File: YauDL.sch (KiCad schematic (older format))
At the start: 32 parts, among them K1 HEATSINK, Q1 IRLZ34N, Q2 IRLZ34N, Q3 AO3401, Q4 AO3401, SW1 SWITCH_INV, T1 Binding post, T2 Binding post, T3 Banana socket, T4 Banana socket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

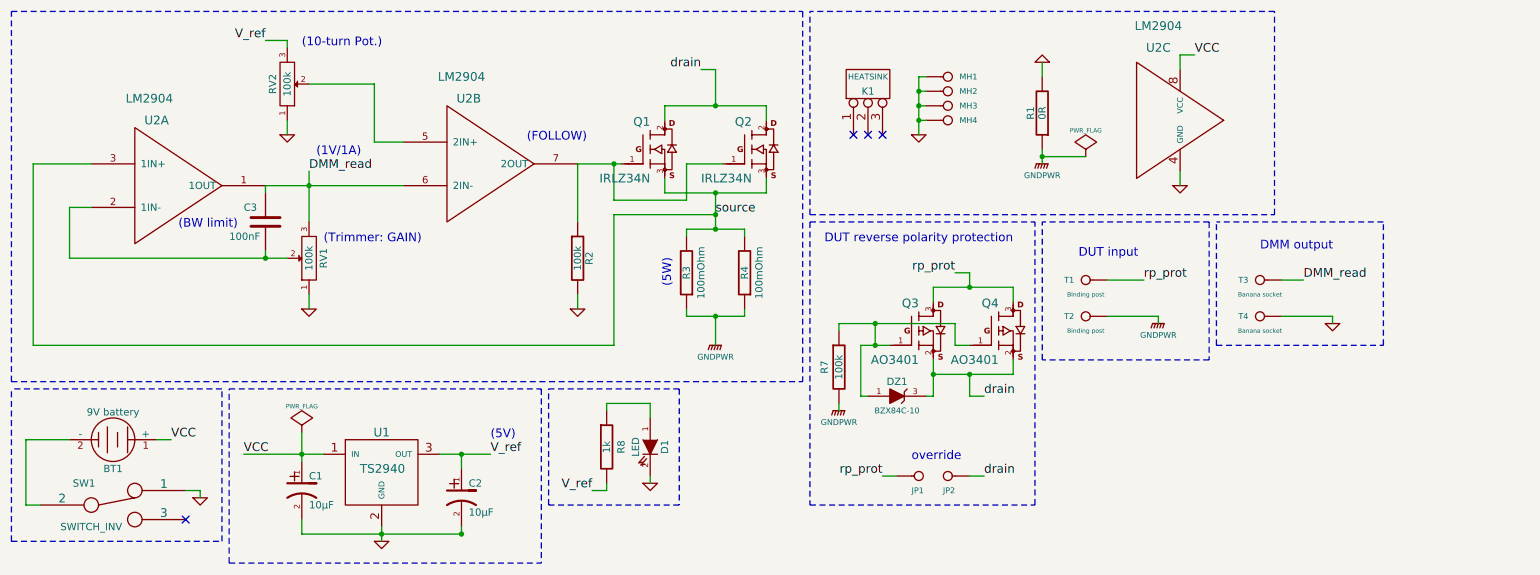
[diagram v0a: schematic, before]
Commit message: Added a low-pass filter (RC=100ms) to the output opamp.
LTSpice simulations indicated oscillation at higher currents.
Hopefully the real thing doesn't require it, but I can bodge it.
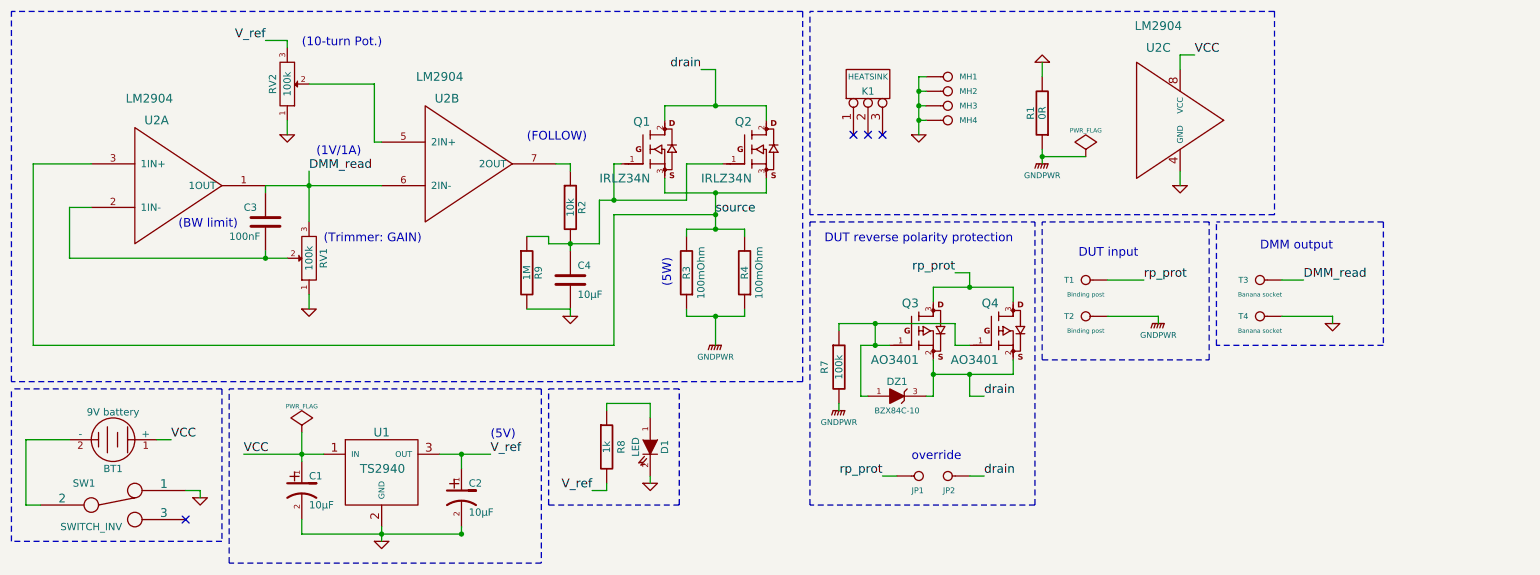
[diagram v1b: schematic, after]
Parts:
- added C4: 10µF, symbol C
- added R9: 1M, symbol R
- R2: value 100k -> 10k
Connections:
- net GND: now also C4.2, R9.2; no longer R2.2
- net at R2.1, U2.7 (2OUT): no longer Q1.1 (G), Q2.1 (G)
- new net: C4.1, Q1.1 (G), Q2.1 (G), R2.2, R9.1
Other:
- moved on the sheet: R2, U2B

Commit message: Had to add some more caps and stuff. The PCB order will go into the trash.
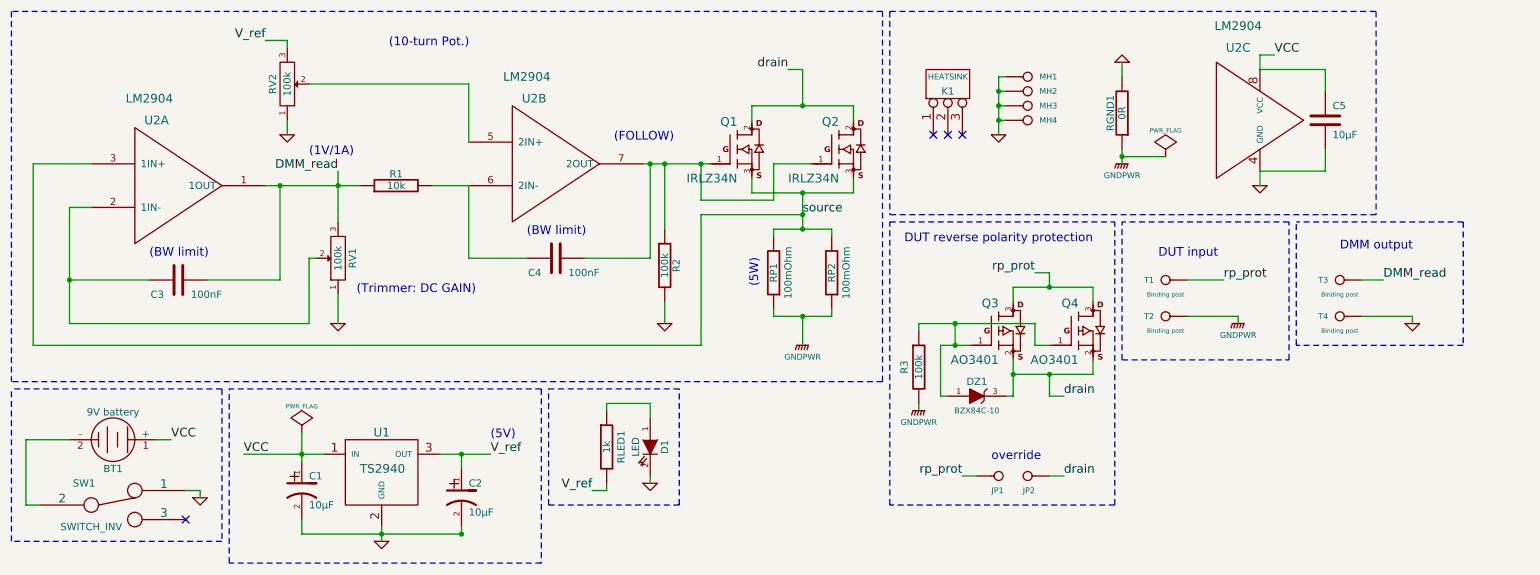
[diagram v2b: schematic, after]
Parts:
- removed R9: 1M, symbol R
- added C5: 10µF, symbol C
- added R1: 10k, symbol R
- C4: value 10µF -> 100nF
- R2: value 10k -> 100k
- T3, T4: value Banana socket -> Binding post
- renumbered R7 to R3, R1 to RGND1, R8 to RLED1, R3 to RP1, R4 to RP2
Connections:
- net DMM_read: now also C3.2, R1.1; no longer C3.1, U2.6 (2IN-)
- net GND: now also R2.2, C5.2; no longer C4.2
- net VCC: now also C5.1
- net at RV1.2, U2.2 (1IN-): now also C3.1; no longer C3.2
- net at R2.1, U2.7 (2OUT): now also C4.2, Q1.1 (G), Q2.1 (G)
- new net: C4.1, R1.2, U2.6 (2IN-)
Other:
- note added: "(Trimmer: DC GAIN)"
- note removed: "(Trimmer: GAIN)"
- moved on the sheet: C3, C4, DZ1, JP1, JP2, K1, MH1, MH2, MH3, MH4, Q1, Q2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

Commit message: New FET: IRL3803 TO-220 (150W dissip.) + some silkscreen tweaks.
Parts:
- Q1, Q2: value IRLZ34N -> IRL3803
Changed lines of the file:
@@
-EESchema Schematic File Version 2  date Sat 09 Jun 2012 03:06:28 PM CEST
+EESchema Schematic File Version 2  date Mon 11 Jun 2012 12:15:04 PM CEST
 LIBS:my_parts
 LIBS:power
@@
 Sheet 1 1
 Title "(Yet) (a)nother (u)seless (D)ummy (Load) - YauDL"
-Date "9 jun 2012"
+Date "11 jun 2012"
 Rev "0.2"
 Comp "2012 - My 2muF - blog.spitzenpfeil.org"
@@
 P 6050 1600
 F 0 "Q2" H 6250 1890 60  0000 R CNN
-F 1 "IRLZ34N" H 6250 1500 60  0000 R CNN
+F 1 "IRL3803" H 6250 1500 60  0000 R CNN
 	1    6050 1600
 	1    0    0    -1
@@
 P 5350 1600
 F 0 "Q1" H 5550 1890 60  0000 R CNN
-F 1 "IRLZ34N" H 5550 1500 60  0000 R CNN
+F 1 "IRL3803" H 5550 1500 60  0000 R CNN
 	1    5350 1600
 	1    0    0    -1

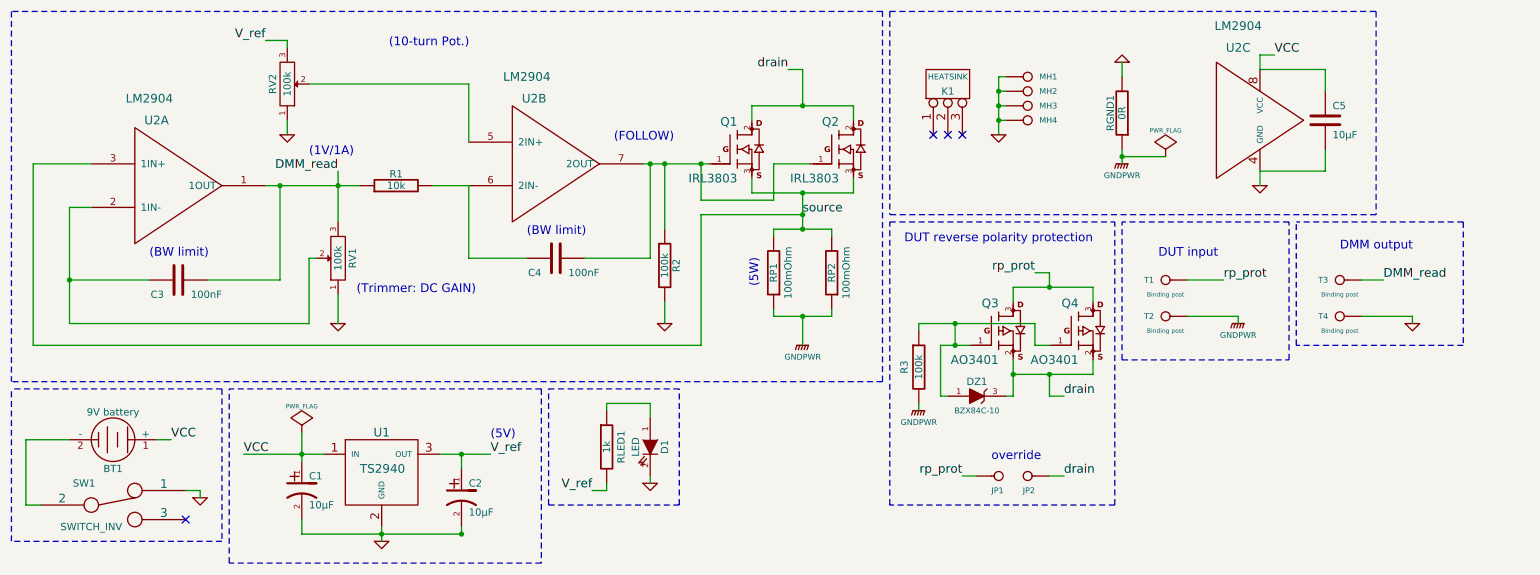
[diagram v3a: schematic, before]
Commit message: Added 2x 10µF ceramic caps across the DUT input.
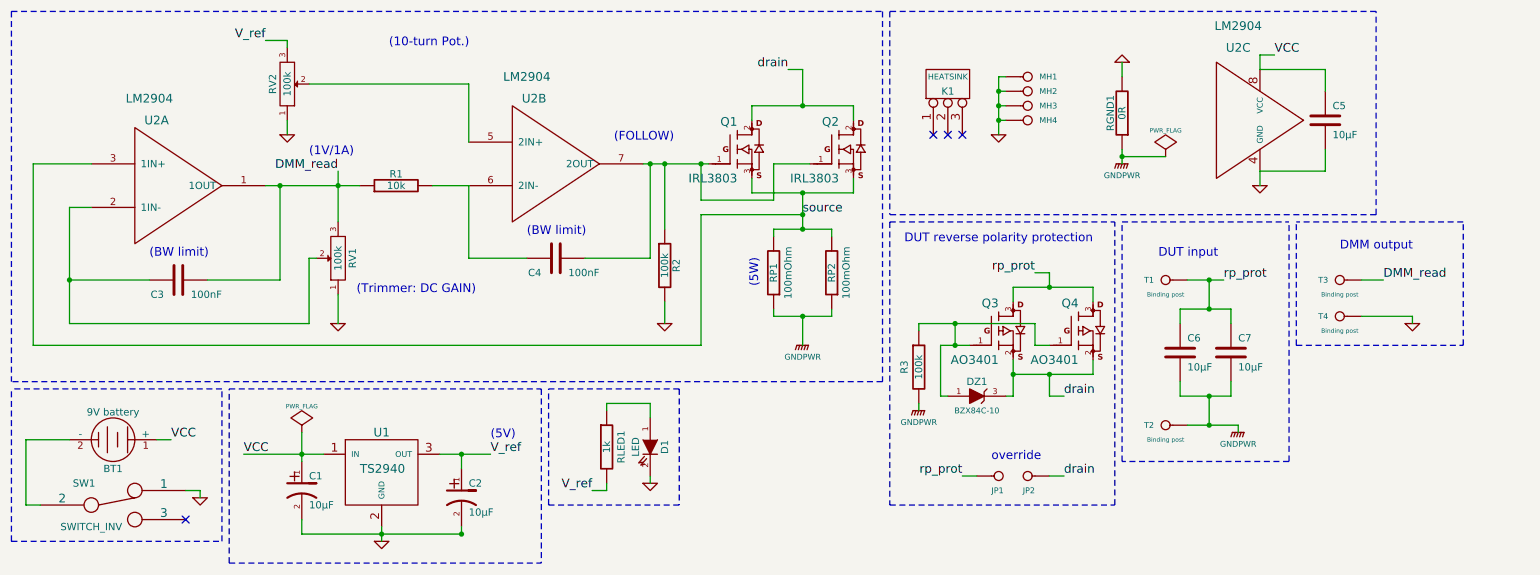
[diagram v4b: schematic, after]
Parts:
- added C6, C7: 10µF, symbol C
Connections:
- net GNDPWR: now also C6.2, C7.2
- net rp_prot: now also C6.1, C7.1
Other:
- moved on the sheet: T2

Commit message: Some fixes:
* The TS2940CW50 voltage regulatr NEEDS tantalum capacitors!

* Changed the LED resistor to 470R to pull minimum current from
  regulator to make it stable. Otherwise it oscillates badly.
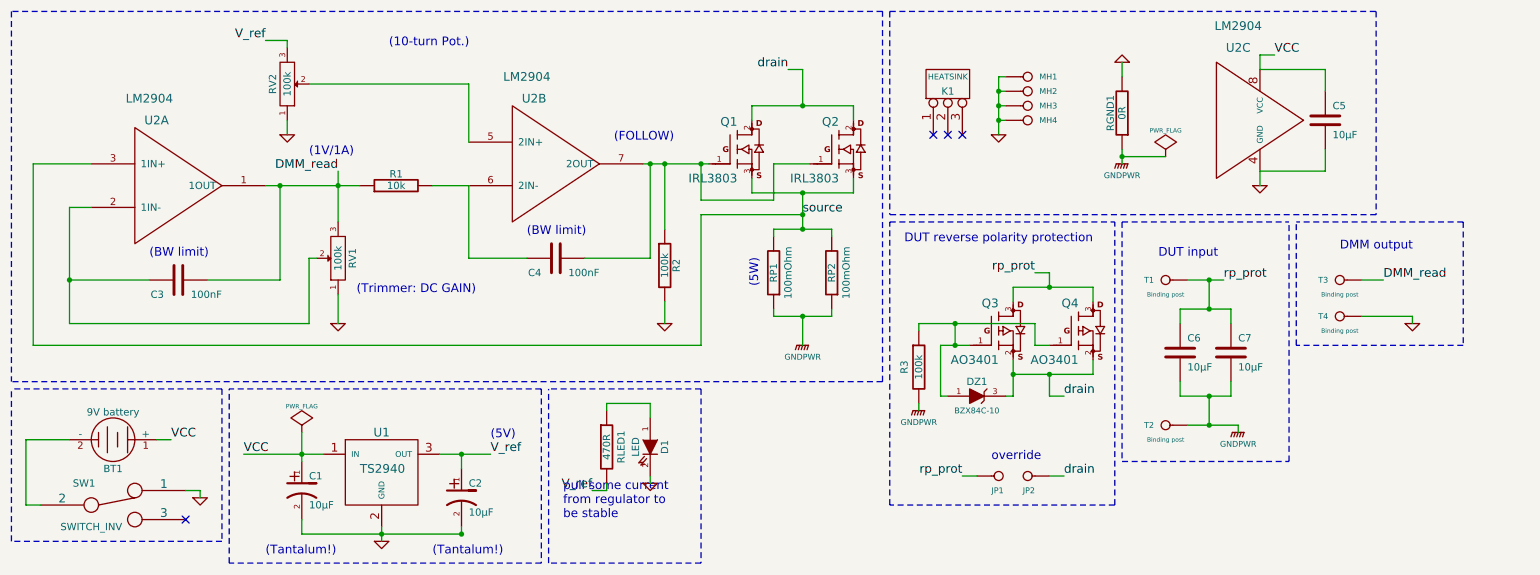
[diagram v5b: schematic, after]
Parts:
- RLED1: value 1k -> 470R
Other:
- note added: "(Tantalum!)"
- note added: "pull some current\nfrom regulator to\nbe stable"

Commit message: The on/off switch now switches VCC instead of GND. Silkscreen tweaks.
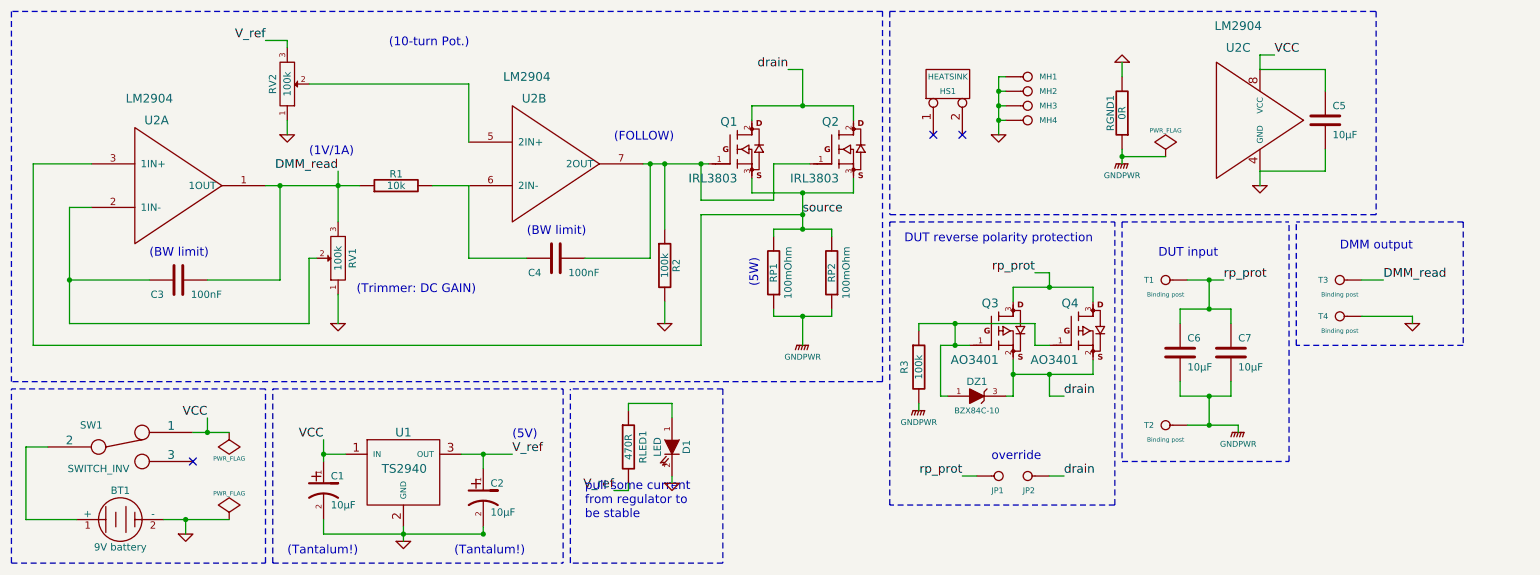
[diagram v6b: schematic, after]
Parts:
- removed K1: HEATSINK, symbol CONN_3
- added HS1: HEATSINK, symbol CONN_2
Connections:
- net GND: now also BT1.2 (-); no longer SW1.1
- net VCC: now also SW1.1; no longer BT1.1 (+)
- net at SW1.2: now also BT1.1 (+); no longer BT1.2 (-)
- no-connect marks 4 -> 3
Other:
- moved on the sheet: BT1, C1, C2, D1, RLED1, SW1, U1

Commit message: Added 2x 100R gate resistors for the power MOSFETs.
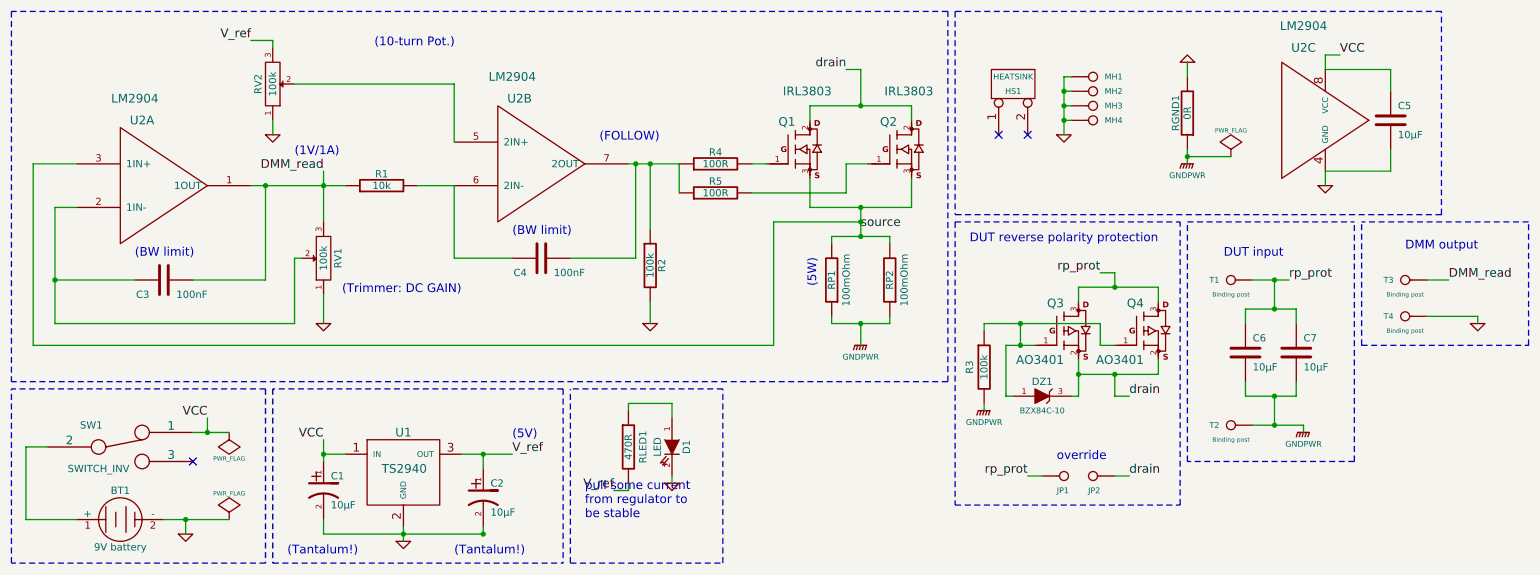
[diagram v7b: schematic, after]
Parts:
- added R4, R5: 100R, symbol R
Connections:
- net at C4.2, R2.1, U2.7 (2OUT): now also R4.1, R5.1; no longer Q1.1 (G), Q2.1 (G)
- new net: Q1.1 (G), R4.2
- new net: Q2.1 (G), R5.2
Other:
- moved on the sheet: C3, C4, C5, C6, C7, DZ1, HS1, JP1, JP2, MH1, MH2, MH3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

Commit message: Replaced the RPP with a beefy Schottky diode (MBR1045).
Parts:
- removed DZ1: BZX84C-10, symbol MADW__ZENER_SOT23
- removed JP1, JP2: CONN_1, symbol CONN_1
- removed Q3, Q4: AO3401, symbol MOSFET_P
- removed R3: 100k, symbol R
- added DS1: MBR1045, symbol MADW__DIODESCH_TO-220
- renumbered R4 to R3, R5 to R4
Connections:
- net drain: now also DS1.1 (C)
- net rp_prot: now also DS1.3 (A)
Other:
- note added: "(45V - 10A)"
- note removed: "DUT reverse polarity protection"
- note removed: "override"
- moved on the sheet: C6, C7, T1, T2, T3, T4
